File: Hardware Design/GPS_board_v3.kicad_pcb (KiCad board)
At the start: 2 copper layers, 50 x 77.5 mm, 17 parts, among them IC2 SN65HVD231QDR, IC3 PIC18F26Q84-I_SS, U5 MAX-M8W

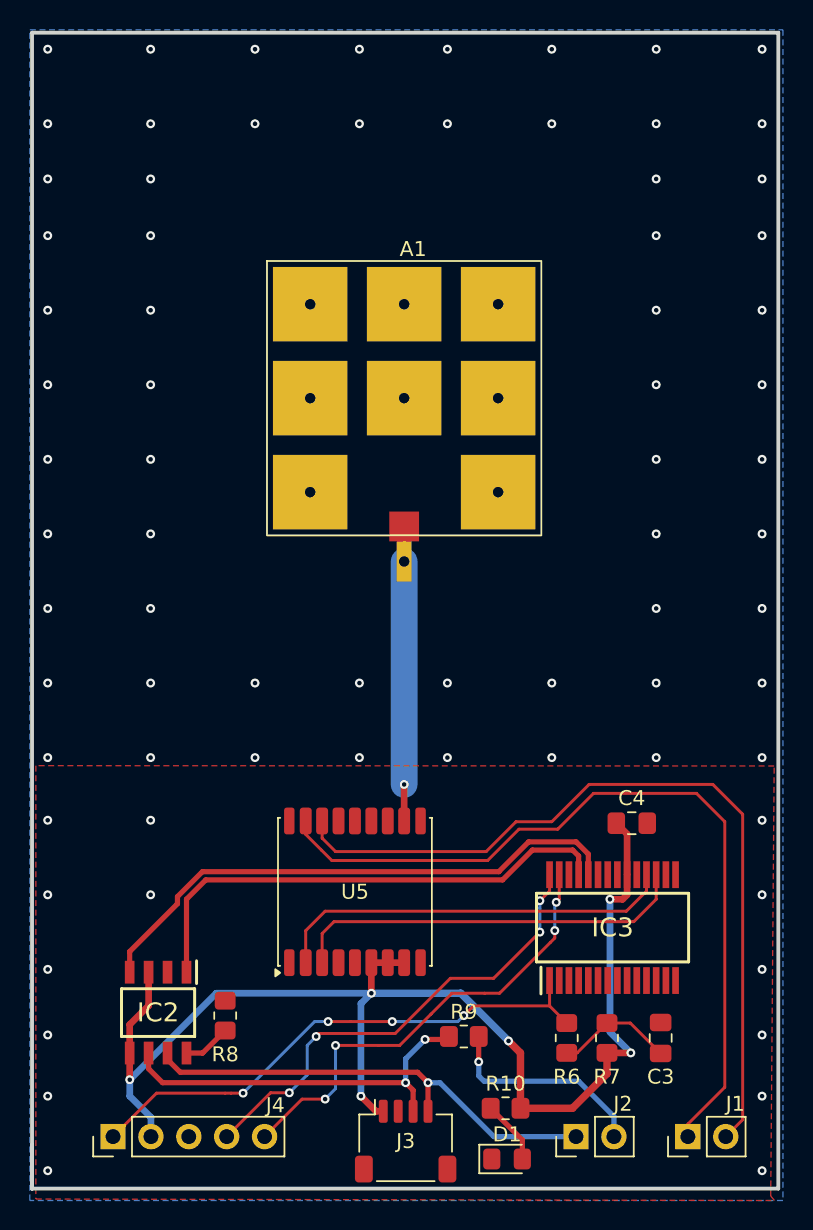
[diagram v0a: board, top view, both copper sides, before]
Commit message: redesigned board for STM32
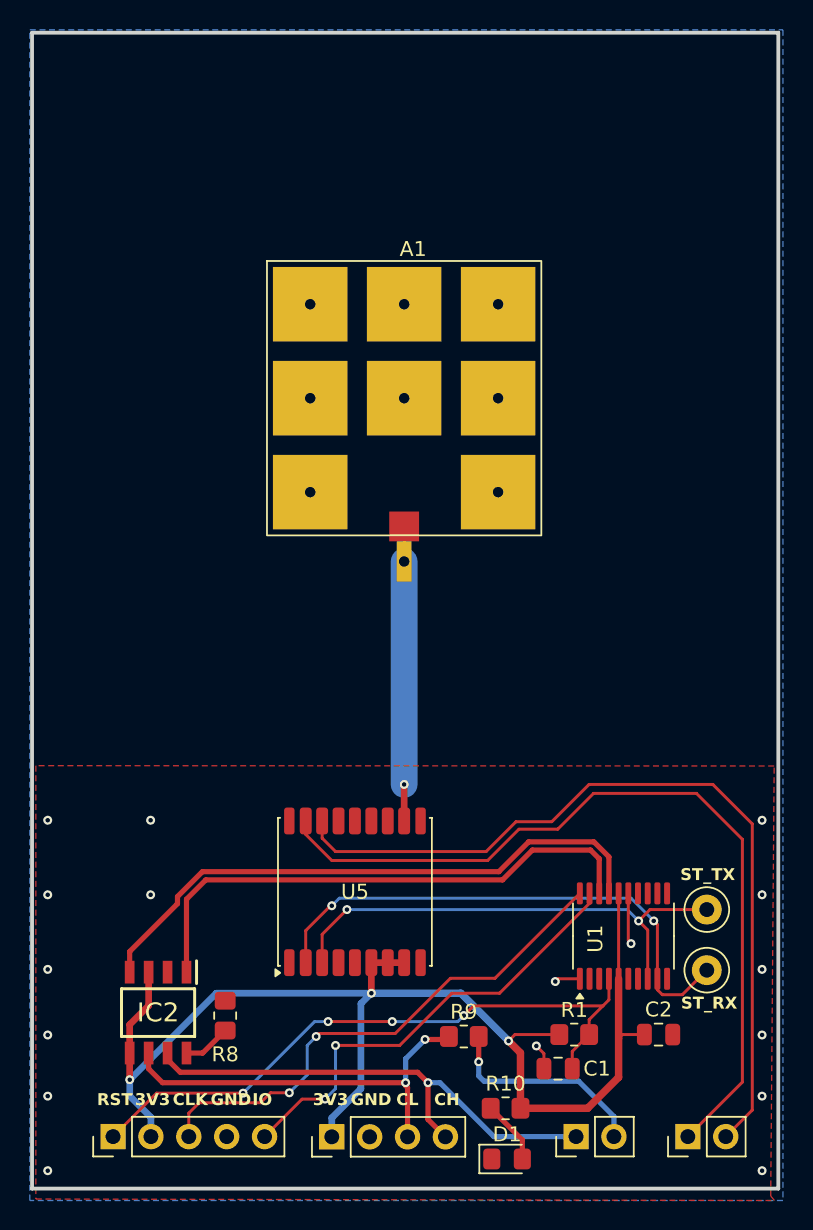
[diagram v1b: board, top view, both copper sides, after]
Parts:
- removed C3, C4: .1uf, Capacitor_SMD:C_0805_2012Metric_Pad1.18x1.45mm_HandSolder
- removed IC3: PIC18F26Q84-I_SS, Package_SO:SOP65P780X200-28N
- removed R6: 120R, Resistor_SMD:R_0805_2012Metric_Pad1.20x1.40mm_HandSolder
- removed R7: 10k, Resistor_SMD:R_0805_2012Metric_Pad1.20x1.40mm_HandSolder
- added C1: .1uF, Capacitor_SMD:C_0805_2012Metric, F.Cu at (157.9, 121.2)
- added C2: .1uF, Capacitor_SMD:C_0805_2012Metric, F.Cu at (164.7, 118.9)
- added R1: 10k, Resistor_SMD:R_0805_2012Metric_Pad1.20x1.40mm_HandSolder, F.Cu at (159.0, 118.9)
- added REF**: TestPoint_Loop_D2.50mm_Drill1.0mm_LowProfile, TestPoint:TestPoint_Loop_D2.50mm_Drill1.0mm_LowProfile, F.Cu at (167.9, 110.5)
- added REF**: TestPoint_Loop_D2.50mm_Drill1.0mm_LowProfile, TestPoint:TestPoint_Loop_D2.50mm_Drill1.0mm_LowProfile, F.Cu at (167.9, 114.6)
- added U1: STM32F042F4Px, Package_SO:TSSOP-20_4.4x6.5mm_P0.65mm, F.Cu at (162.3, 112.3)
- J3: footprint Connector_JST:JST_SH_SM04B-SRSS-TB_1x04-1MP_P1.00mm_Horizontal -> Connector_PinHeader_2.54mm:PinHeader_1x04_P2.54mm_Vertical
- moved J3 4.96 mm to (142.7, 125.7), turned to 90 degrees
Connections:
- J4 pad 1: MCLR/VPP -> STM_RST
- J4 pad 3: GND -> SWCLK
- J4 pad 4: ICSPDAT -> GND
- J4 pad 5: ICSPCLK -> SWDIO
- U5 pad 2: UART_TX -> STM_UART_RX
- U5 pad 3: UART_RX -> STM_UART_TX
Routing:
- net STM_RST: track 0.00 -> 43.5 mm, vias 0 -> 4
- net MCLR/VPP: track 36.2 -> 0.00 mm, vias 4 -> 0
- net STM_UART_RX: track 0.00 -> 35.9 mm, vias 0 -> 2
- net SWCLK: track 0.00 -> 35.1 mm, vias 0 -> 2
- net STM_UART_TX: track 0.00 -> 33.1 mm, vias 0 -> 2
- net ICSPDAT: track 32.0 -> 0.00 mm, vias 4 -> 0
- net ICSPCLK: track 31.0 -> 0.00 mm, vias 4 -> 0
- net SWDIO: track 0.00 -> 30.6 mm, vias 0 -> 2
- net UART_TX: track 27.2 -> 0.00 mm
- net UART_RX: track 27.0 -> 0.00 mm
- net Net-(C3-Pad2): track 7.97 -> 0.00 mm
- net GND: track 0.00 -> 6.90 mm, vias 74 -> 17
- net CAN_RX: track 37.2 -> 39.7 mm
- net CAN_TX: track 34.0 -> 36.5 mm
- net CANH: track 31.9 -> 34.1 mm
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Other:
- outline, holes or cut-outs redrawn
- board text added: "3V3"
- board text added: "CH"
- board text added: "CL"
- board text added: "CLK"
- board text added: "GND"
- board text added: "IO"
- board text added: "RST"
- board text added: "ST_RX"
- board text added: "ST_TX"

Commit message: fixed gerbers & bom
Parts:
- added REF**: TestPoint_Loop_D2.50mm_Drill1.0mm_LowProfile, TestPoint:TestPoint_Loop_D2.50mm_Drill1.0mm_LowProfile, F.Cu at (126.8, 111.6)
- added REF**: TestPoint_Loop_D2.50mm_Drill1.0mm_LowProfile, TestPoint:TestPoint_Loop_D2.50mm_Drill1.0mm_LowProfile, F.Cu at (135.4, 111.4)
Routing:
- net CAN_RX: track 39.7 -> 42.9 mm
- net CAN_TX: track 36.5 -> 39.6 mm
- net SWDIO: vias 2 -> 1
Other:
- board text added: "CANRX"
- board text added: "CANTX"
